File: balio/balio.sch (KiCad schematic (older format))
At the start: 69 parts, among them J1 IN1, J10 OUT4, J11 OUT3, J12 OUT4, J13 MON3, J14 MON4, J15 MON3, J16 MON4, J17 POWER, J18 POWER, J2 IN2, J3 IN1, J4 IN2, J5 OUT1, J6 OUT2, J7 IN3, J8 IN4, J9 OUT3, U1 INA134, U2 INA134, U3 TL072, U4 TL072

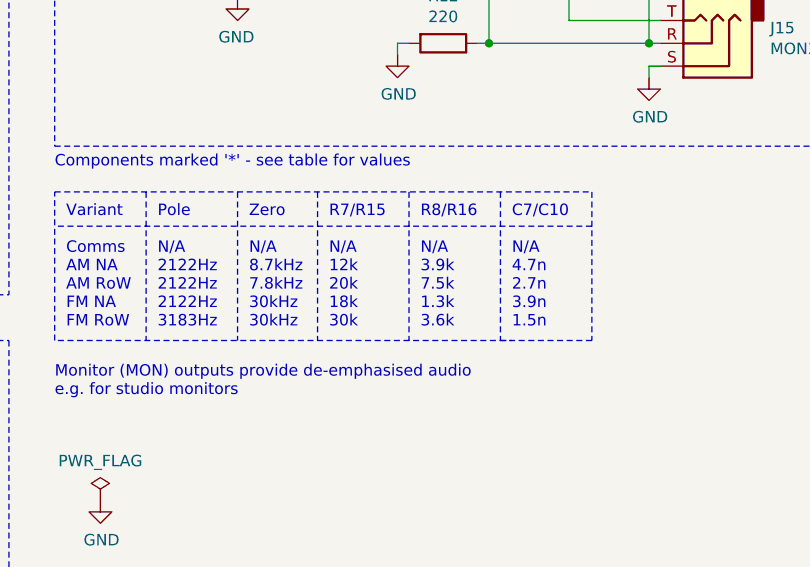
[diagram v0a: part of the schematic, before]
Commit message: Changed Balanced IO card de-emphasis circuit in AM RoW variant to match pre-emphasis changes in previous commit
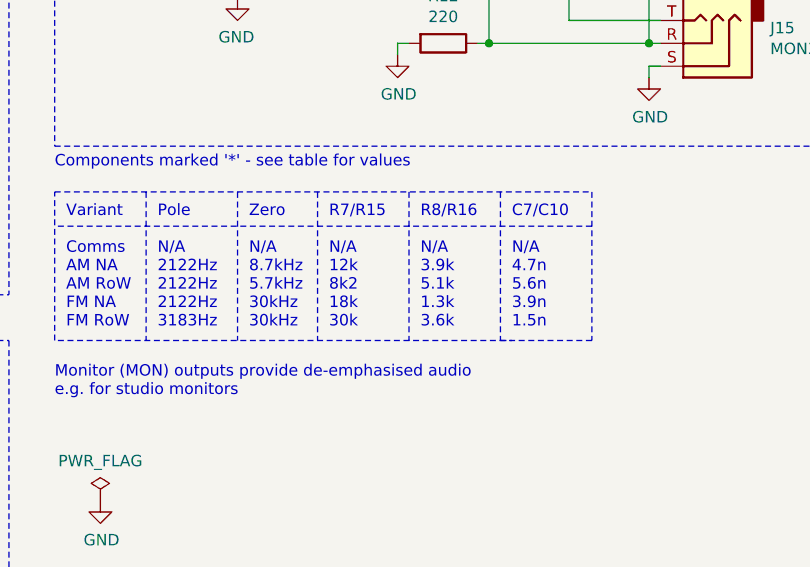
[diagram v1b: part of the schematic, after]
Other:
- note added: "C7/C10\n\nN/A\n4.7n\n5.6n\n3.9n\n1.5n"
- note added: "R7/R15\n\nN/A\n12k\n8k2\n18k\n30k"
- note added: "R8/R16\n\nN/A\n3.9k\n5.1k\n1.3k\n3.6k"
- note added: "Zero\n\nN/A\n8.7kHz\n5.7kHz\n30kHz\n30kHz"
- note removed: "C7/C10\n\nN/A\n4.7n\n2.7n\n3.9n\n1.5n"
- note removed: "R7/R15\n\nN/A\n12k\n20k\n18k\n30k"
- note removed: "R8/R16\n\nN/A\n3.9k\n7.5k\n1.3k\n3.6k"
- note removed: "Zero\n\nN/A\n8.7kHz\n7.8kHz\n30kHz\n30kHz"
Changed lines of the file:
@@
 Text Notes 4450 5000 0    50   ~ 0
 Pole\n\nN/A\n2122Hz\n2122Hz\n2122Hz\n3183Hz
-Text Notes 4850 5000 0    50   ~ 0
-Zero\n\nN/A\n8.7kHz\n7.8kHz\n30kHz\n30kHz
 Text Notes 5600 5000 0    50   ~ 0
-R8/R16\n\nN/A\n3.9k\n7.5k\n1.3k\n3.6k
+R8/R16\n\nN/A\n3.9k\n5.1k\n1.3k\n3.6k
 Text Notes 5200 5000 0    50   ~ 0
-R7/R15\n\nN/A\n12k\n20k\n18k\n30k
+R7/R15\n\nN/A\n12k\n8k2\n18k\n30k
 Text Notes 6000 5000 0    50   ~ 0
-C7/C10\n\nN/A\n4.7n\n2.7n\n3.9n\n1.5n
+C7/C10\n\nN/A\n4.7n\n5.6n\n3.9n\n1.5n
 Wire Notes Line style solid
 	4000 4400 6350 4400
@@
 	1    0    0    -1
 $EndComp
+Text Notes 4850 5000 0    50   ~ 0
+Zero\n\nN/A\n8.7kHz\n5.7kHz\n30kHz\n30kHz
 $EndSCHEMATC
